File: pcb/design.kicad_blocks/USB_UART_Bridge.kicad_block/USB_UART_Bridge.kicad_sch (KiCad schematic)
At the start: 18 parts, among them J2 USB_C_Receptacle, U2 MCP2221A-I/ST, U3 AP2112K-3.3

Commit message: Added USB-C receptacle 3D model.
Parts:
- J2: footprint Connector_USB:USB_C_Receptacle_Amphenol_12401548E4-2A -> pcb:USB_C_Receptacle_Amphenol_12401548E4-2A
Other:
- note added: "USB-UART Bridge (V7 : USB-C Model)."
- note removed: "USB-UART Bridge (V6 : USB-C)."
- moved on the sheet: C13, C15, C16, C17, D1, D2, D3, D4, J2, JP3, R16, R19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

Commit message: `USB-UART Bridge (V8 : Enable with solder-bridge).`
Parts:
- removed JP3: Jumper_2_Small_Bridged, Connector_PinHeader_2.54mm:PinHeader_1x02_P2.54mm_Vertical, symbol Jumper:Jumper_2_Small_Bridged
- added JP1: SolderJumper_2_Open, Jumper:SolderJumper-2_P1.3mm_Open_RoundedPad1.0x1.5mm, symbol Jumper:SolderJumper_2_Open
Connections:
- net at C13.1, C15.1, J2.A4 (VBUS)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: now also JP1.1 (A)
- net at U3.3 (EN): now also JP1.2 (B)
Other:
- note added: "USB-UART Bridge (V8 : Enable with solder-bridge)."
- note removed: "USB-UART Bridge (V7 : USB-C Model)."
- moved on the sheet: C13, C15, C16, C17, D1, D2, D3, D4, J2, R16, R19, R20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

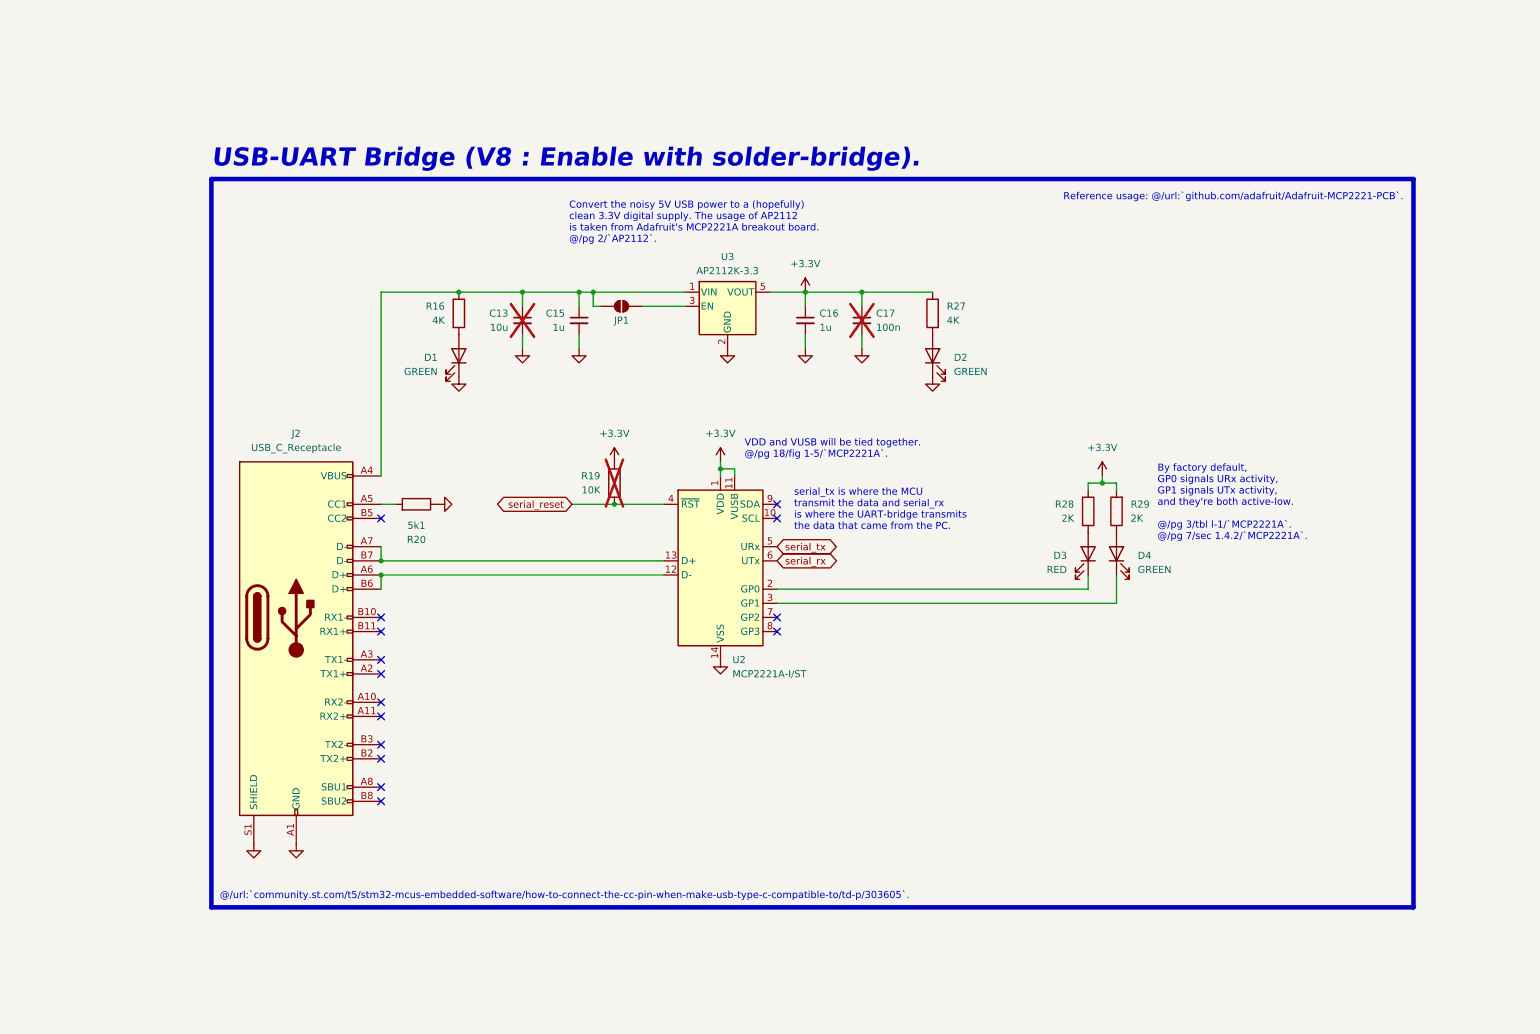
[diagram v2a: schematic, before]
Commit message: Replaced `12401548E4#2A` with `12401598E4#2A` for `USB_UART_Bridge`.
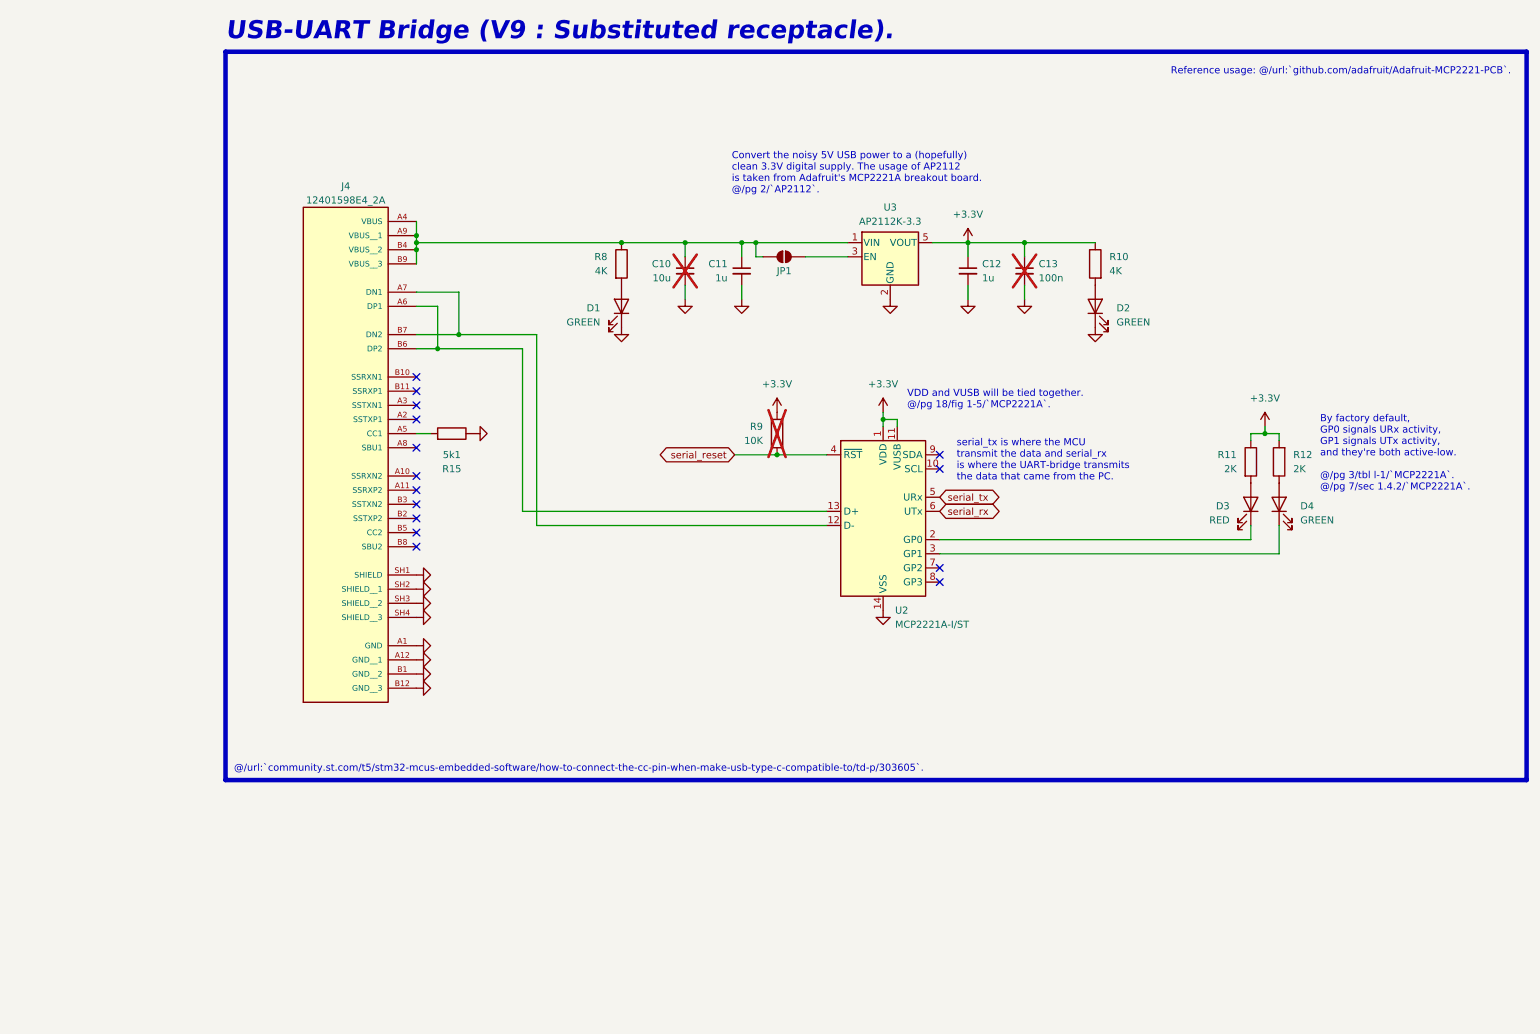
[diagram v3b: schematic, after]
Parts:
- removed J2: USB_C_Receptacle, pcb:USB_C_Receptacle_Amphenol_12401548E4-2A, symbol Connector:USB_C_Receptacle
- removed R20: 5k1, Resistor_SMD:R_1206_3216Metric_Pad1.30x1.75mm_HandSolder, symbol Device:R
- added J4: 12401598E4_2A, pcb:AMPHENOL_12401598E4_2A, symbol 12401598E4_2A:12401598E4_2A
- added R15: 5k1, Resistor_SMD:R_1206_3216Metric_Pad1.30x1.75mm_HandSolder, symbol Device:R
- renumbered C13 to C10, C15 to C11, C16 to C12, C17 to C13, R27 to R10, R28 to R11, R29 to R12, R16 to R8, R19 to R9
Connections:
- net GND: now also J4.A1 (GND), J4.A12 (GND__1), J4.B1 (GND__2), J4.B12 (GND__3), J4.SH1 (SHIELD), J4.SH2 (SHIELD__1), J4.SH3 (SHIELD__2), J4.SH4 (SHIELD__3), R15.1
- net at C10.1, C11.1, JP1.1 (A)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: now also J4.A4 (VBUS), J4.A9 (VBUS__1), J4.B4 (VBUS__2), J4.B9 (VBUS__3)
- net at U2.12 (D-): now also J4.A7 (DN1), J4.B7 (DN2)
- net at U2.13 (D+): now also J4.A6 (DP1), J4.B6 (DP2)
- new net: J4.A5 (CC1), R15.2
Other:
- note added: "USB-UART Bridge (V9 : Substituted receptacle)."
- note removed: "USB-UART Bridge (V8 : Enable with solder-bridge)."
- moved on the sheet: C10, C11, C12, C13, D1, D2, D3, D4, JP1, R10, R11, R12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
